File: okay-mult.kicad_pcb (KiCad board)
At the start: 2 copper layers, 44.2 x 111 mm, 45 parts, among them J1 Conn_02x05_Odd_Even, J10 Conn_01x02_Female, J11 Conn_01x02_Female, J12 Conn_01x02_Male, J13 Conn_01x02_Male, J14 Thonkiconn, J15 Thonkiconn, J16 Thonkiconn, J17 Thonkiconn, J18 Conn_01x01_Female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

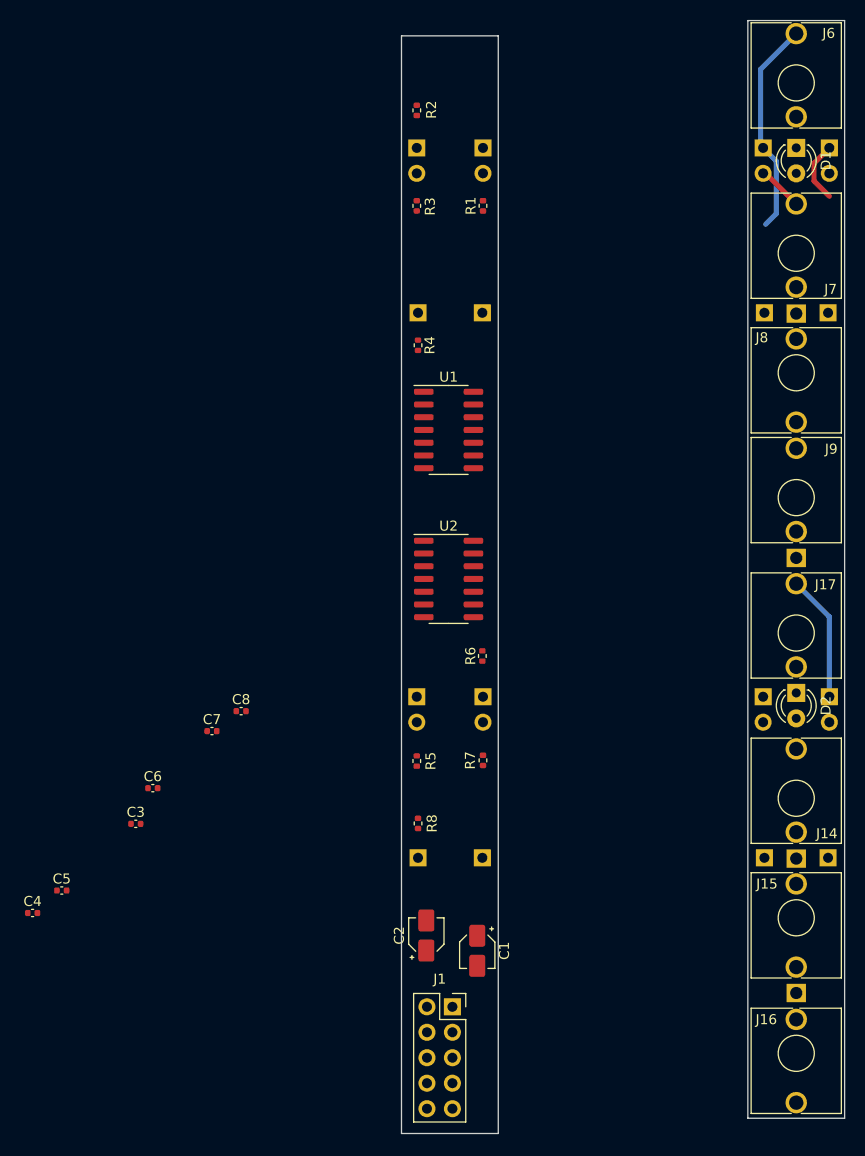
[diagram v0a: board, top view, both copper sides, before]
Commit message: Bigger fatter traces
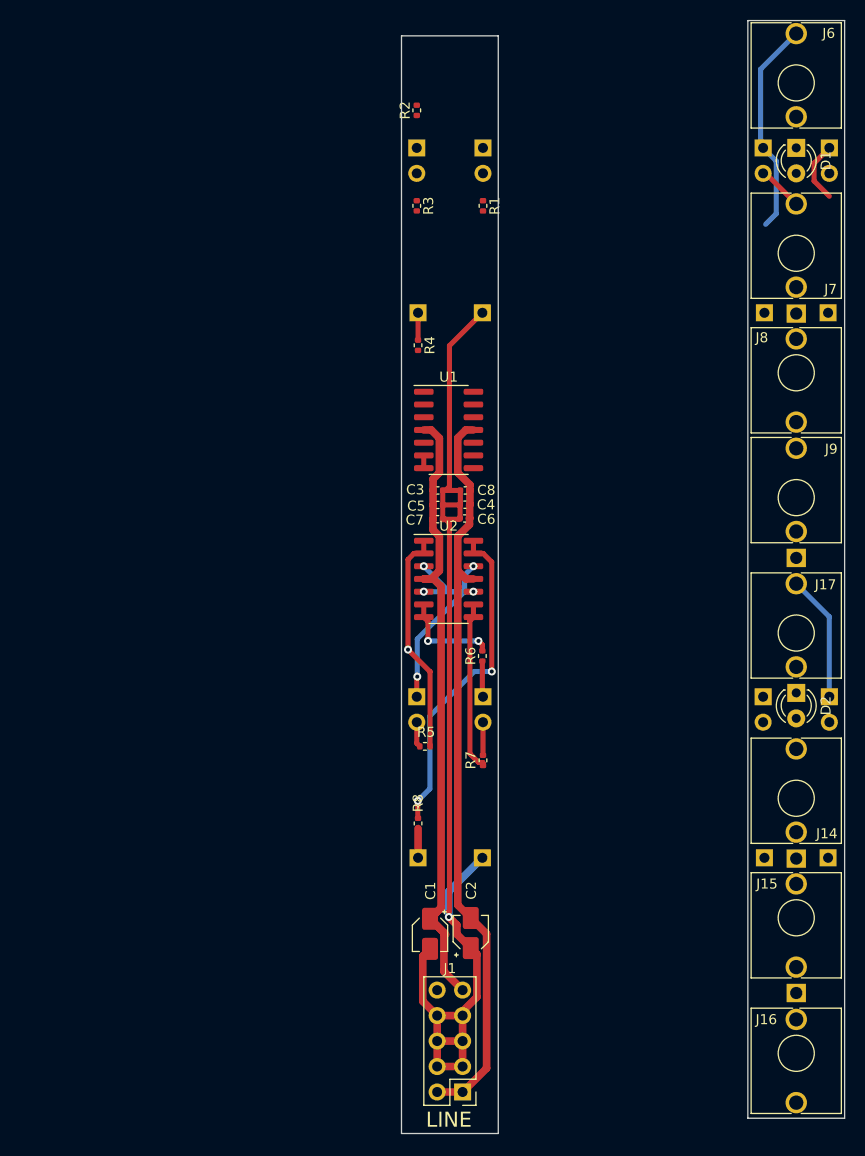
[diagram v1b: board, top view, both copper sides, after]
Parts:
- J1: footprint Connector_PinSocket_2.54mm:PinSocket_2x05_P2.54mm_Vertical -> Connector_PinHeader_2.54mm:PinHeader_2x05_P2.54mm_Vertical
- moved C4 59.3 mm to (119.1, 75.5)
- moved C5 53.7 mm to (116.4, 75.5)
- moved C3 44.9 mm to (116.4, 74.0)
- moved C6 41.1 mm to (119.1, 76.8)
- moved C8 31.4 mm to (119.1, 74.0)
- moved C7 30.9 mm to (116.4, 76.9)
- moved J1 8.56 mm to (118.9, 134.0), turned to 180 degrees
- moved C1 5.01 mm to (115.6, 118.3)
- moved C2 4.44 mm to (119.7, 118.2)
- moved R5 1.67 mm to (115.1, 99.6), turned to 0 degrees
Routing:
- net GND: track 2.03 -> 116.8 mm, vias 0 -> 1
- net /-12V: track 0.00 -> 74.8 mm
- net /+12V: track 0.00 -> 65.2 mm
- net Net-(R8-Pad2): track 0.00 -> 33.1 mm, vias 0 -> 2
- net /IN_B: track 12.6 -> 39.0 mm, vias 0 -> 5
- net Net-(R5-Pad2): track 0.00 -> 22.6 mm, vias 0 -> 1
- net Net-(R7-Pad2): track 0.00 -> 17.0 mm
- net Net-(R6-Pad2): track 0.00 -> 10.0 mm, vias 0 -> 2
- net /F: track 0.00 -> 3.58 mm
- net /G: track 0.00 -> 3.30 mm
- net /LED_B: track 0.00 -> 2.92 mm
- net /LED_A: track 0.00 -> 2.73 mm
- net /E: track 0.64 -> 3.17 mm
- net Net-(R2-Pad2): track 0.00 -> 1.27 mm
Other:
- board text added: "LINE"
